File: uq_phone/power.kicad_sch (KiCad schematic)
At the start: 32 parts, among them J1 USB4105-GF-A, J2 S3B-PH-SM4-TB_LF__SN_, U1 MCP73871-2CCI_ML, U2 TPS62162DSGR, U3 BQ27441DRZR-G1A

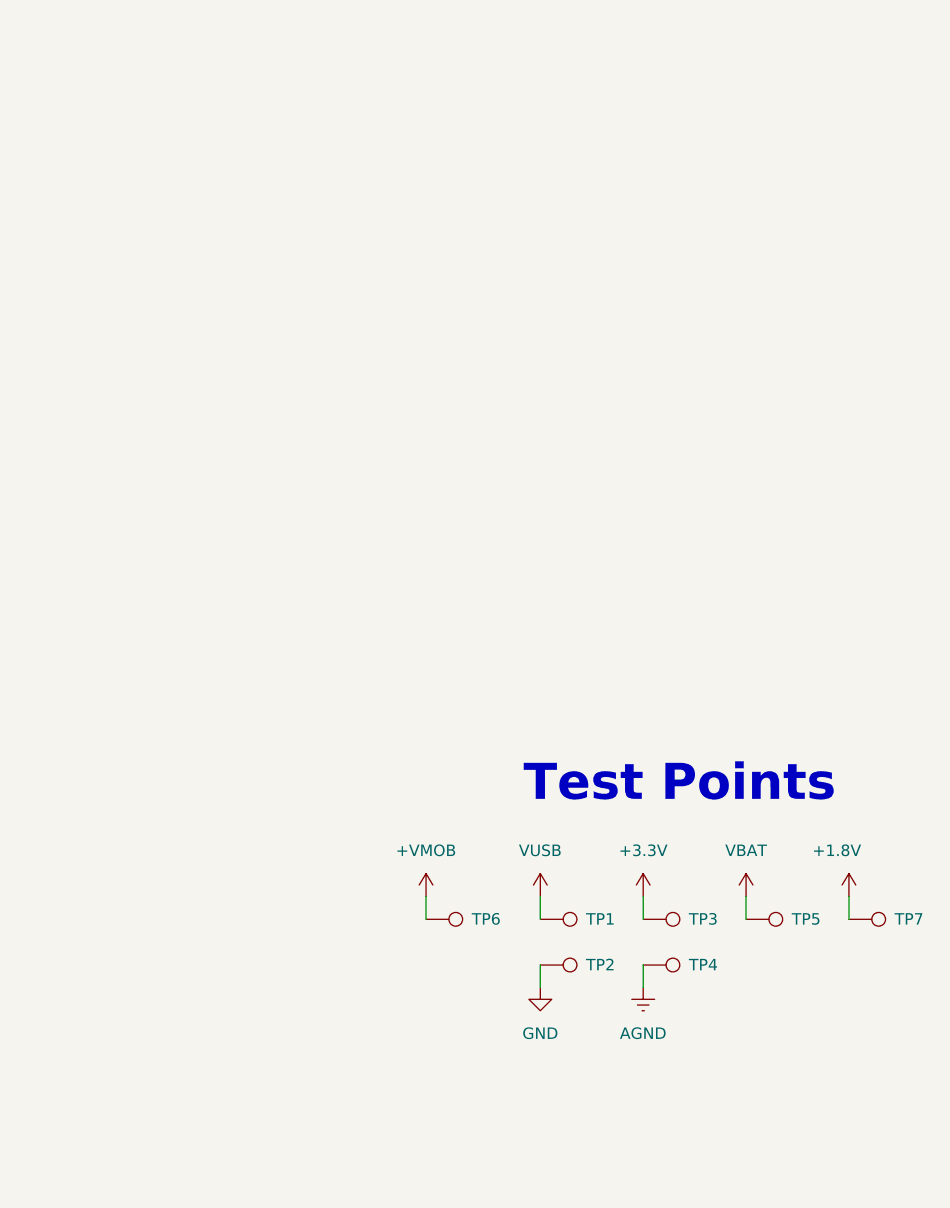
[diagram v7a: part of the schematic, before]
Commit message: Clean up and add DNP
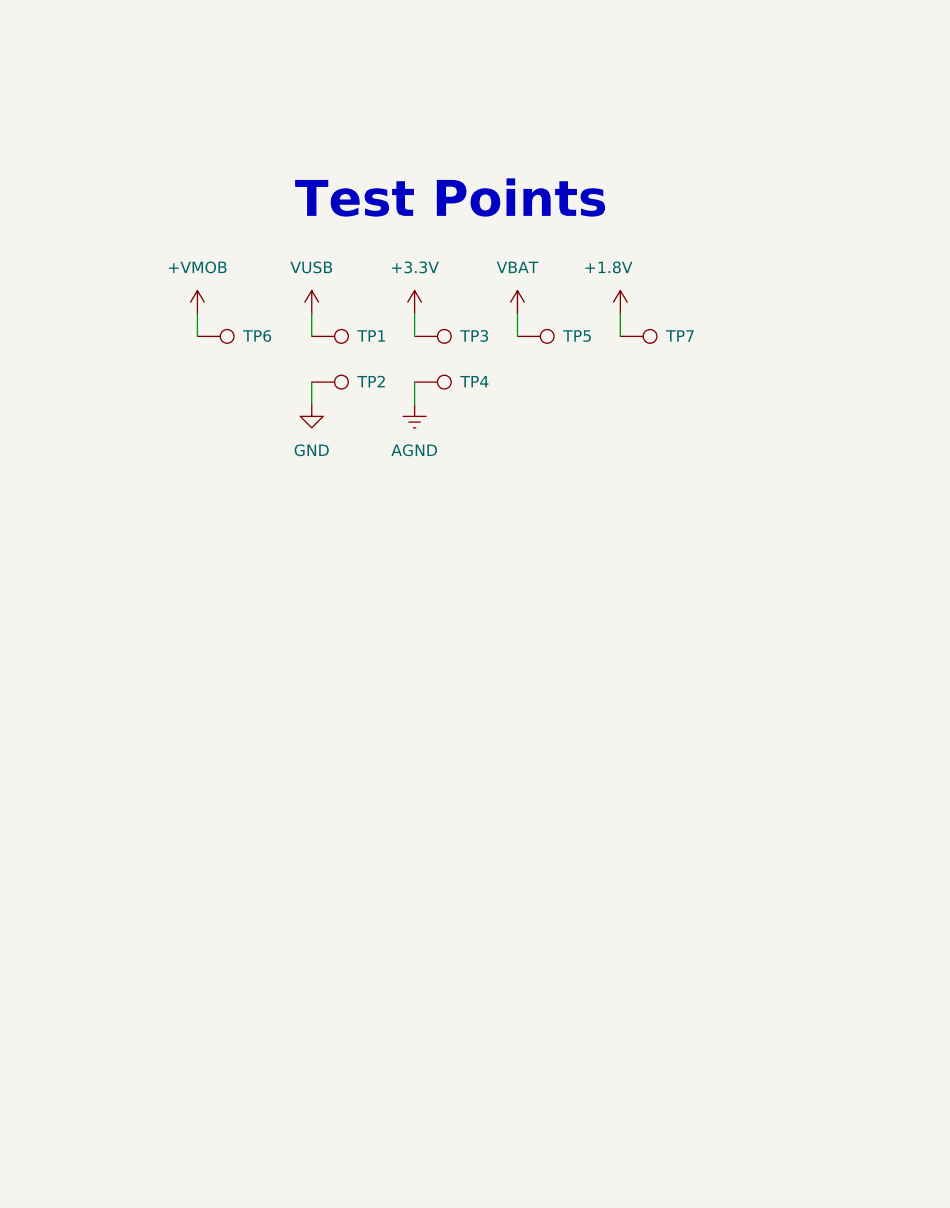
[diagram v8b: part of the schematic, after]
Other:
- moved on the sheet: TP1, TP2, TP3, TP4, TP5, TP6, TP7
